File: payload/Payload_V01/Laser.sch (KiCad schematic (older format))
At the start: 4 parts, among them U3 MLD203CLN

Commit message: added footprints and 3d models
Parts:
- LD1: footprint (none) -> OptoDevice:LaserDiode_TO18-D5.6-3
- R10: footprint (none) -> Resistor_SMD:R_0603_1608Metric_Pad1.05x0.95mm_HandSolder
- RV1: footprint (none) -> Potentiometer_SMD:Potentiometer_Vishay_TS53YJ_Vertical
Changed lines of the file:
@@
 F 0 "RV1" V 4795 3850 50  0000 C CNN
 F 1 "10k" V 4886 3850 50  0000 C CNN
-F 2 "" H 5000 3850 50  0001 C CNN
+F 2 "Potentiometer_SMD:Potentiometer_Vishay_TS53YJ_Vertical" H 5000 3850 50  0001 C CNN
 F 3 "~" H 5000 3850 50  0001 C CNN
 	1    5000 3850
@@
 F 0 "LD1" V 6854 4147 50  0000 L CNN
 F 1 "DJ532-40" V 6945 4147 50  0000 L CNN
-F 2 "" H 6950 4000 50  0001 C CNN
+F 2 "OptoDevice:LaserDiode_TO18-D5.6-3" H 6950 4000 50  0001 C CNN
 F 3 "" H 6950 4000 50  0001 C CNN
 	1    6950 4000
@@
 F 0 "R10" V 6445 3850 50  0000 C CNN
 F 1 "1k" V 6536 3850 50  0000 C CNN
-F 2 "" V 6690 3840 50  0001 C CNN
+F 2 "Resistor_SMD:R_0603_1608Metric_Pad1.05x0.95mm_HandSolder" V 6690 3840 50  0001 C CNN
 F 3 "~" H 6650 3850 50  0001 C CNN
 	1    6650 3850

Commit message: added driver footprint and model
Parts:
- U3: footprint (none) -> Payload_V01:MLD203CLN
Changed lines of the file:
@@
 F 0 "U3" H 5850 4415 50  0000 C CNN
 F 1 "MLD203CLN" H 5850 4324 50  0000 C CNN
-F 2 "" H 5850 3700 50  0001 C CNN
+F 2 "Payload_V01:MLD203CLN" H 5850 3700 50  0001 C CNN
 F 3 "" H 5850 3700 50  0001 C CNN
 	1    5850 3700

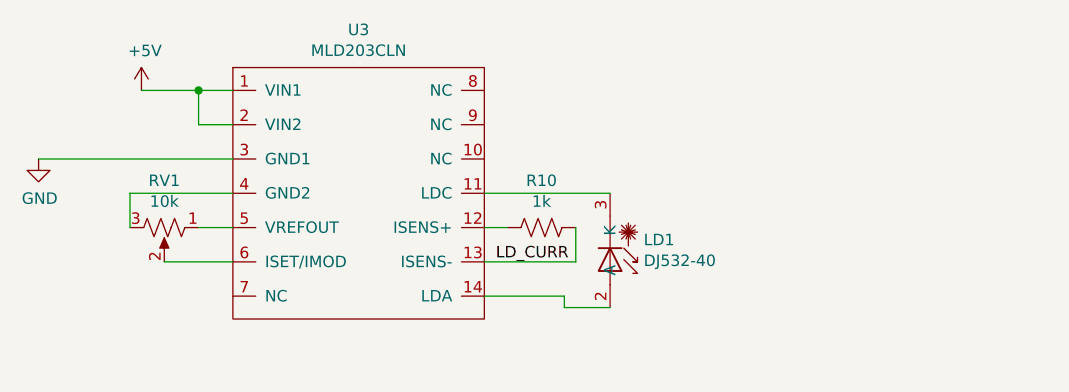
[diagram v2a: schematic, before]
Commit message: added some more pins
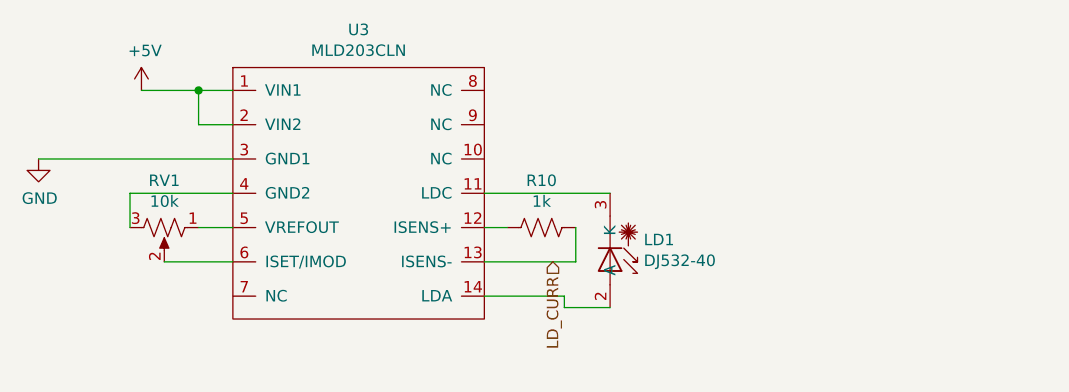
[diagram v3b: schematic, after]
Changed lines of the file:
@@
 Wire Wire Line
 	6800 4000 6400 4000
-Text Label 6450 4000 0    50   ~ 0
+Text HLabel 6700 4000 3    50   Input ~ 0
 LD_CURR
 $EndSCHEMATC

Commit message: fixed laser driver
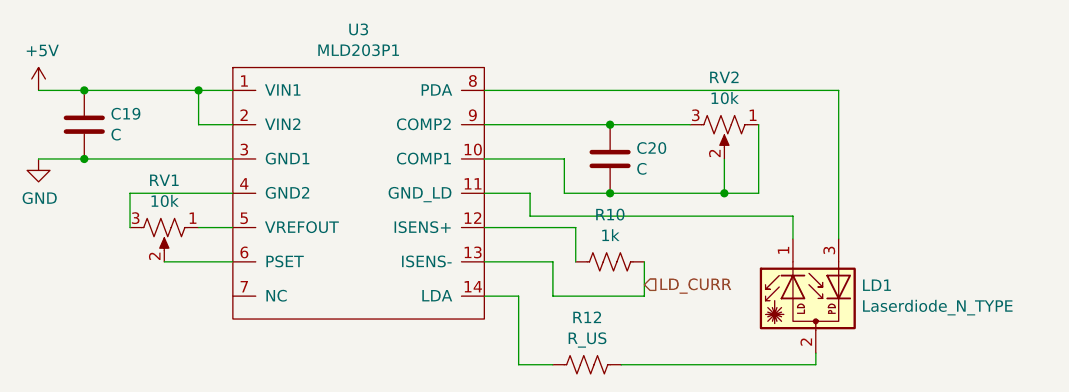
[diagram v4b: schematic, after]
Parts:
- removed LD1: DJ532-40, OptoDevice:LaserDiode_TO18-D5.6-3, symbol Payload_V01:DJ532-40
- removed U3: MLD203CLN, Payload_V01:MLD203CLN, symbol Payload_V01:MLD203CLN
- added C19, C20: C, Capacitor_SMD:C_0603_1608Metric_Pad1.05x0.95mm_HandSolder, symbol Device:C
- added LD1: Laserdiode_N_TYPE, OptoDevice:LaserDiode_TO18-D5.6-3, symbol Device:Laserdiode_N_TYPE
- added R12: R_US, Resistor_SMD:R_0603_1608Metric_Pad1.05x0.95mm_HandSolder, symbol Device:R_US
- added RV2: 10k, Potentiometer_SMD:Potentiometer_Vishay_TS53YJ_Vertical, symbol Device:R_POT_US
- added U3: MLD203P1, Payload_V01:MLD203CLN, symbol Payload_V01:MLD203P1
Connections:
- net +5V: now also C19.1, U3.1 (VIN1), U3.2 (VIN2)
- net GND: now also C19.2, U3.3 (GND1)
- net LD_CURR: now also U3.13 (ISENS-)
- net at RV1.1: now also U3.5 (VREFOUT)
- net at RV1.2: now also U3.6 (PSET)
- net at RV1.3: now also U3.4 (GND2)
- net at R10.2: now also U3.12 (ISENS+)
- new net: C20.2, RV2.1, RV2.2, U3.10 (COMP1)
- new net: LD1.1, U3.11 (GND_LD)
- new net: R12.2, U3.14 (LDA)
- new net: LD1.3, U3.8 (PDA)
- new net: C20.1, RV2.3, U3.9 (COMP2)
- new net: LD1.2, R12.1
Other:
- moved on the sheet: R10
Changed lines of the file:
@@
 $EndComp
-$Comp
-L power:+5V #PWR0128
-U 1 1 5F18CD3D
-P 4900 3250
-F 0 "#PWR0128" H 4900 3100 50  0001 C CNN
-F 1 "+5V" H 4915 3423 50  0000 C CNN
-F 2 "" H 4900 3250 50  0001 C CNN
-F 3 "" H 4900 3250 50  0001 C CNN
-	1    4900 3250
-	1    0    0    -1
-$EndComp
-Wire Wire Line
-	4900 3250 5150 3250
-Wire Wire Line
-	5150 3250 5150 3400
-Wire Wire Line
-	5150 3400 5300 3400
-Connection ~ 5150 3250
-Wire Wire Line
-	5150 3250 5300 3250
 $Comp
 L Device:R_POT_US RV1
@@
 $EndComp
 Wire Wire Line
-	4450 3550 5300 3550
-Wire Wire Line
 	5150 3850 5300 3850
 Wire Wire Line
@@
 	5300 4000 5000 4000
 $Comp
-L Payload_V01:DJ532-40 LD1
-U 1 1 5F1DD2C7
+L Device:R_US R10
+U 1 1 5F1E131A
 P 6950 4000
-F 0 "LD1" V 6854 4147 50  0000 L CNN
-F 1 "DJ532-40" V 6945 4147 50  0000 L CNN
-F 2 "OptoDevice:LaserDiode_TO18-D5.6-3" H 6950 4000 50  0001 C CNN
-F 3 "" H 6950 4000 50  0001 C CNN
+F 0 "R10" V 6745 4000 50  0000 C CNN
+F 1 "1k" V 6836 4000 50  0000 C CNN
+F 2 "Resistor_SMD:R_0603_1608Metric_Pad1.05x0.95mm_HandSolder" V 6990 3990 50  0001 C CNN
+F 3 "~" H 6950 4000 50  0001 C CNN
 	1    6950 4000
 	0    1    1    0
 $EndComp
+Text HLabel 7100 4100 2    50   Input ~ 0
+LD_CURR
 $Comp
-L Payload_V01:MLD203CLN U3
-U 1 1 5F1DFA85
+L Payload_V01:MLD203P1 U3
+U 1 1 5F2CE4A1
 P 5850 3700
 F 0 "U3" H 5850 4415 50  0000 C CNN
-F 1 "MLD203CLN" H 5850 4324 50  0000 C CNN
+F 1 "MLD203P1" H 5850 4324 50  0000 C CNN
 F 2 "Payload_V01:MLD203CLN" H 5850 3700 50  0001 C CNN
 F 3 "" H 5850 3700 50  0001 C CNN
@@
 	1    0    0    -1
 $EndComp
-Wire Wire Line
-	6400 4150 6750 4150
-Wire Wire Line
-	6750 4150 6750 4200
-Wire Wire Line
-	6750 4200 6950 4200
-Wire Wire Line
-	6400 3700 6950 3700
 $Comp
-L Device:R_US R10
-U 1 1 5F1E131A
-P 6650 3850
-F 0 "R10" V 6445 3850 50  0000 C CNN
-F 1 "1k" V 6536 3850 50  0000 C CNN
-F 2 "Resistor_SMD:R_0603_1608Metric_Pad1.05x0.95mm_HandSolder" V 6690 3840 50  0001 C CNN
-F 3 "~" H 6650 3850 50  0001 C CNN
-	1    6650 3850
+L power:+5V #PWR0128
+U 1 1 5F18CD3D
+P 4450 3250
+F 0 "#PWR0128" H 4450 3100 50  0001 C CNN
+F 1 "+5V" H 4465 3423 50  0000 C CNN
+F 2 "" H 4450 3250 50  0001 C CNN
+F 3 "" H 4450 3250 50  0001 C CNN
+	1    4450 3250
+	1    0    0    -1
+$EndComp
+$Comp
+L Device:Laserdiode_N_TYPE LD1
+U 1 1 5F2CFBA5
+P 7850 4200
+F 0 "LD1" V 7946 4000 50  0000 R CNN
+F 1 "Laserdiode_N_TYPE" V 7855 4000 50  0000 R CNN
+F 2 "OptoDevice:LaserDiode_TO18-D5.6-3" H 7850 4275 50  0001 C CNN
+F 3 "http://www.egismos.disonhu.com/laser/diode-package.htm" H 7900 4100 50  0001 C CNN
+	1    7850 4200
+	0    -1   -1   0
+$EndComp
+$Comp
+L Device:R_US R12
+U 1 1 5F2D21D6
+P 6850 4450
+F 0 "R12" V 6645 4450 50  0000 C CNN
+F 1 "R_US" V 6736 4450 50  0000 C CNN
+F 2 "Resistor_SMD:R_0603_1608Metric_Pad1.05x0.95mm_HandSolder" V 6890 4440 50  0001 C CNN
+F 3 "~" H 6850 4450 50  0001 C CNN
+	1    6850 4450
+	0    1    1    0
+$EndComp
+$Comp
+L Device:C C20
+U 1 1 5F2D42F0
+P 6950 3550
+F 0 "C20" H 7065 3596 50  0000 L CNN
+F 1 "C" H 7065 3505 50  0000 L CNN
+F 2 "Capacitor_SMD:C_0603_1608Metric_Pad1.05x0.95mm_HandSolder" H 6988 3400 50  0001 C CNN
+F 3 "~" H 6950 3550 50  0001 C CNN
+	1    6950 3550
+	1    0    0    -1
+$EndComp
+$Comp
+L Device:R_POT_US RV2
+U 1 1 5F2D456E
+P 7450 3400
+F 0 "RV2" V 7245 3400 50  0000 C CNN
+F 1 "10k" V 7336 3400 50  0000 C CNN
+F 2 "Potentiometer_SMD:Potentiometer_Vishay_TS53YJ_Vertical" H 7450 3400 50  0001 C CNN
+F 3 "~" H 7450 3400 50  0001 C CNN
+	1    7450 3400
 	0    1    1    0
 $EndComp
 Wire Wire Line
-	6400 3850 6500 3850
+	6400 3400 6950 3400
+Wire Wire Line
+	6950 3400 7300 3400
+Connection ~ 6950 3400
+Wire Wire Line
+	7600 3400 7600 3700
+Wire Wire Line
+	7600 3700 7450 3700
+Wire Wire Line
+	6950 3700 6750 3700
+Wire Wire Line
+	6750 3700 6750 3550
+Wire Wire Line
+	6750 3550 6400 3550
+Connection ~ 6950 3700
+Wire Wire Line
+	7450 3550 7450 3700
+Connection ~ 7450 3700
+Wire Wire Line
+	7450 3700 6950 3700
+Wire Wire Line
+	6400 3700 6600 3700
+Wire Wire Line
+	6600 3700 6600 3800
+Wire Wire Line
+	6600 3800 7750 3800
+Wire Wire Line
+	7750 3800 7750 3900
+Wire Wire Line
+	7950 3900 7950 3250
+Wire Wire Line
+	7950 3250 6400 3250
+Wire Wire Line
+	7850 4400 7850 4450
+Wire Wire Line
+	7850 4450 7000 4450
+Wire Wire Line
+	6700 4450 6550 4450
+Wire Wire Line
+	6550 4450 6550 4150
+Wire Wire Line
+	6400 4150 6550 4150
+Wire Wire Line
+	6400 3850 6800 3850
 Wire Wire Line
 	6800 3850 6800 4000
 Wire Wire Line
-	6800 4000 6400 4000
-Text HLabel 6700 4000 3    50   Input ~ 0
-LD_CURR
+	7100 4000 7100 4150
+Wire Wire Line
+	7100 4150 6700 4150
+Wire Wire Line
+	6700 4150 6700 4000
+Wire Wire Line
+	6700 4000 6400 4000
+$Comp
+L Device:C C19
+U 1 1 5F2DBA53
+P 4650 3400
+F 0 "C19" H 4765 3446 50  0000 L CNN
+F 1 "C" H 4765 3355 50  0000 L CNN
+F 2 "Capacitor_SMD:C_0603_1608Metric_Pad1.05x0.95mm_HandSolder" H 4688 3250 50  0001 C CNN
+F 3 "~" H 4650 3400 50  0001 C CNN
+	1    4650 3400
+	1    0    0    -1
+$EndComp
+Wire Wire Line
+	5300 3550 4650 3550
+Connection ~ 4650 3550
+Wire Wire Line
+	4650 3550 4450 3550
+Wire Wire Line
+	4650 3250 5150 3250
+Wire Wire Line
+	5150 3250 5150 3400
+Wire Wire Line
+	5150 3400 5300 3400
+Connection ~ 5150 3250
+Wire Wire Line
+	5150 3250 5300 3250
+Wire Wire Line
+	4650 3250 4450 3250
+Connection ~ 4650 3250
 $EndSCHEMATC
